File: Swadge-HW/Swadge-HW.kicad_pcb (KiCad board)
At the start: 2 copper layers, 140 x 94.2 mm, 90 parts, among them J1 SAO, J2 PJ-307C, J3 PGM, P1 USB_C_Plug_USB2.0, Q1 Q_PMOS_GSD, SW1 YTS-D003-1A, SW2 YTS-D003-1A, SW3 YTS-D003-1A, SW4 YTS-D003-1A, SW5 YTS-D003-1A, SW6 YTS-D003-1A, SW7 B3FS-4002P, SW8 B3FS-4002P, SW9 SW_SPDT_1825232-1, U1 ESP32-S2-MINI-1, U2 RB017A1505A, U3 MT3410, U5 RB017A1505A_Connector, U6 LSM6DSL, U7 GENERIC_LDO_2.8, U8 FM8002A, U9 INGHAi_GSPK2307P-8R1W

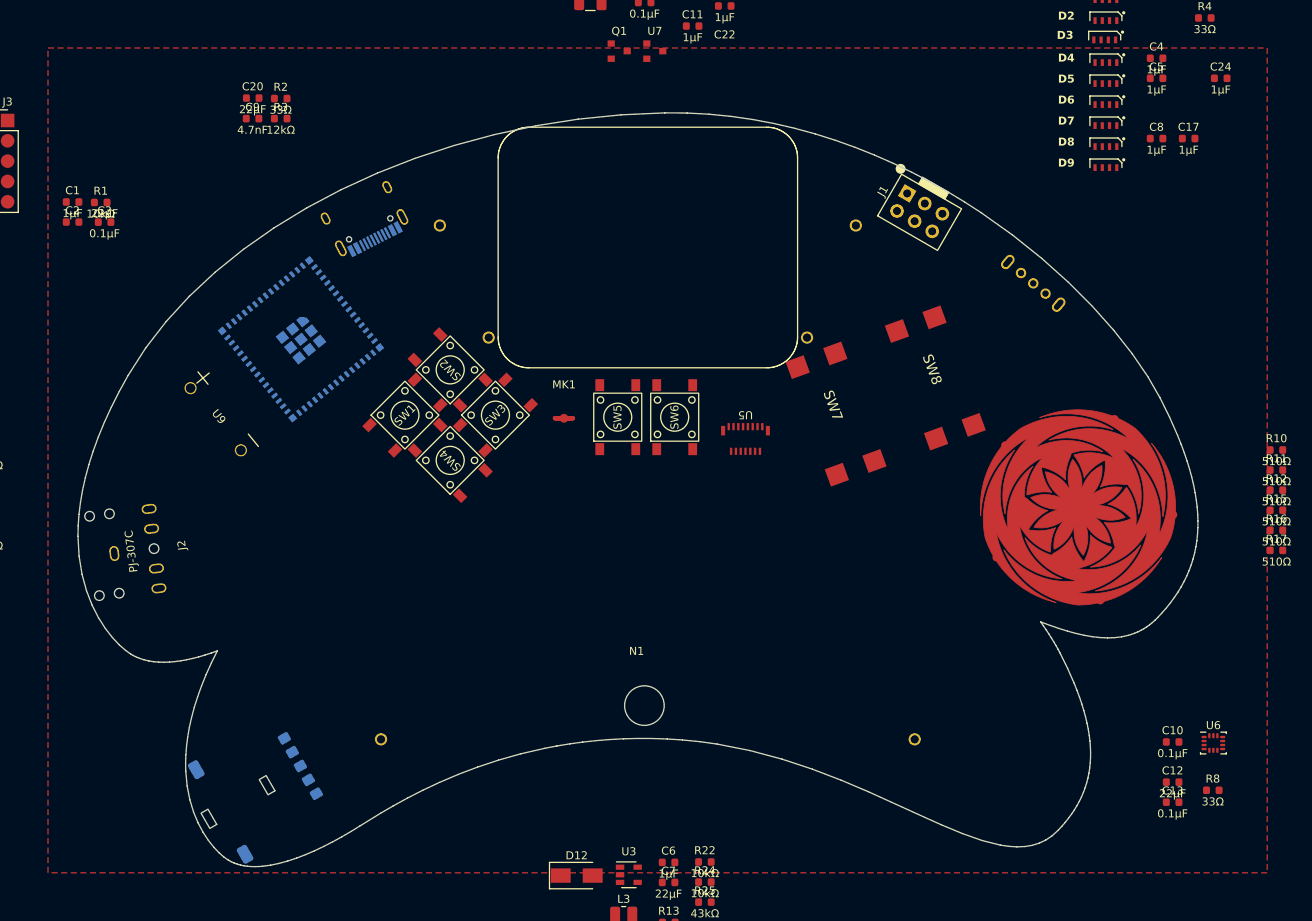
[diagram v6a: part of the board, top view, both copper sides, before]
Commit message: Updated to new board shape
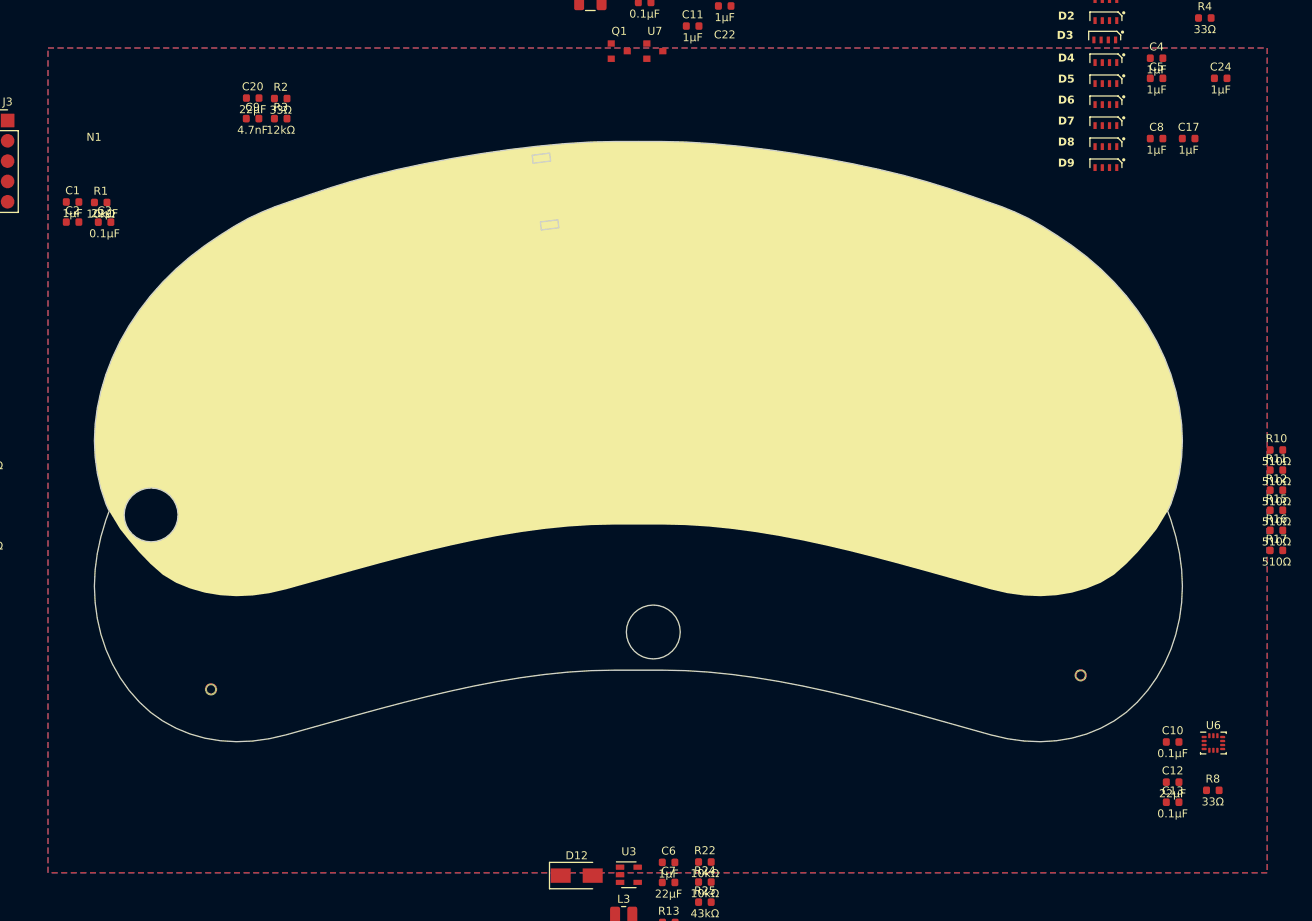
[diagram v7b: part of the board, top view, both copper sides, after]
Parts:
- J2: moved to B.Cu
- N1: value Acrylic Sausage -> Board Outline; footprint Swadge_Hotdog:Sausage -> Swadge_Hotdog:hotdog-outline
- moved N1 93.4 mm to (82.0, 62.4)
- moved RV1 85.4 mm to (138.4, 68.7), turned to -173 degrees
- moved P1 64.0 mm to (179.2, 69.1), turned to -15 degrees
- moved J2 60.0 mm to (124.4, 69.1), turned to -167 degrees
- moved U1 57.1 mm to (163.8, 76.2), turned to 173 degrees
- moved U5 39.1 mm to (139.6, 68.6), turned to 0 degrees
- moved J1 36.3 mm to (147.5, 65.5), turned to 90 degrees
- moved SW6 32.9 mm to (122.0, 101.7), turned to -170 degrees
- moved U9 31.9 mm to (122.0, 77.3), turned to -40 degrees
- moved BT2 28.0 mm to (151.9, 101.0)
- moved SW5 26.9 mm to (123.3, 108.7), turned to -170 degrees
- moved BT3 22.2 mm to (198.6, 104.1)
- moved BT1 22.2 mm to (103.3, 105.9)
- moved SW3 21.0 mm to (111.6, 92.4)
- moved SW2 21.0 mm to (105.9, 86.7)
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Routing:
- added copper zone on B.Cu, net (none)
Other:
- board size 140 x 94.2 mm -> 136 x 75 mm

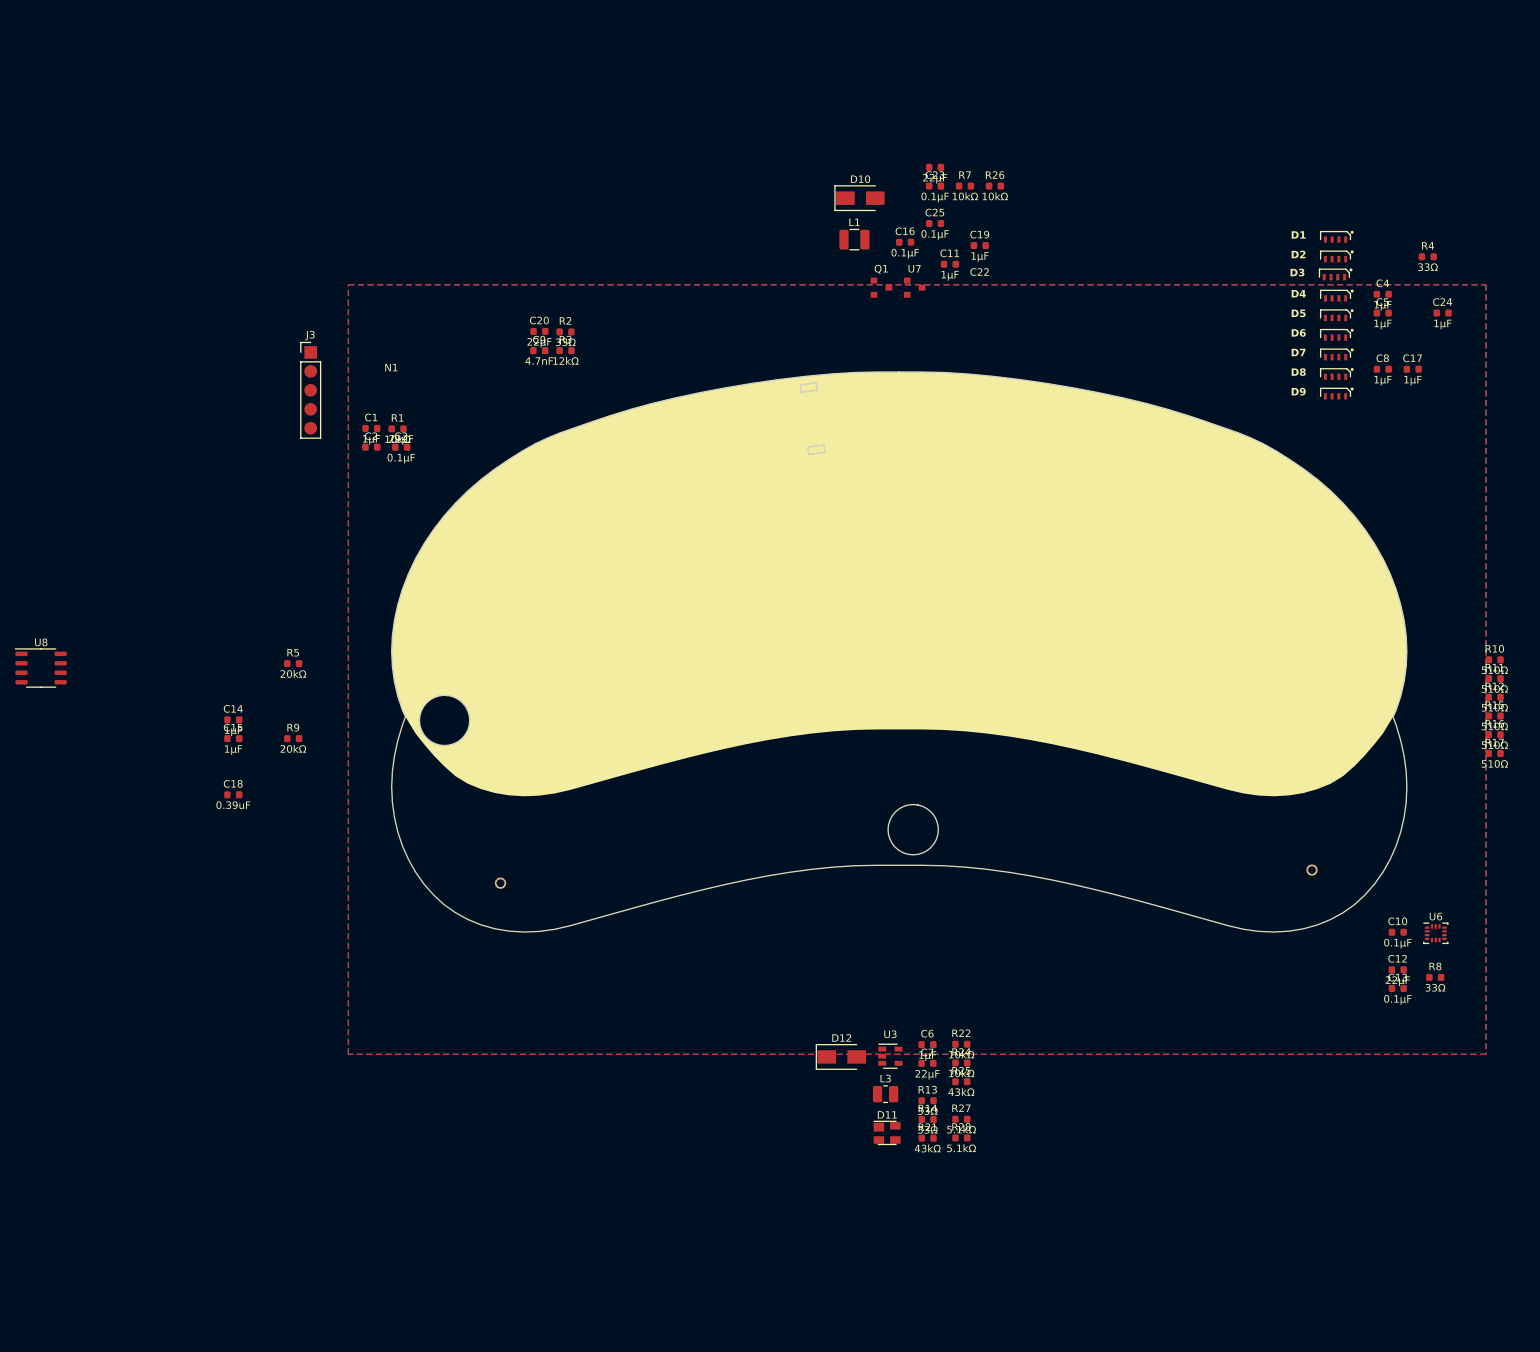
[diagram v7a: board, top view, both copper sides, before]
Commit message: Placed big parts
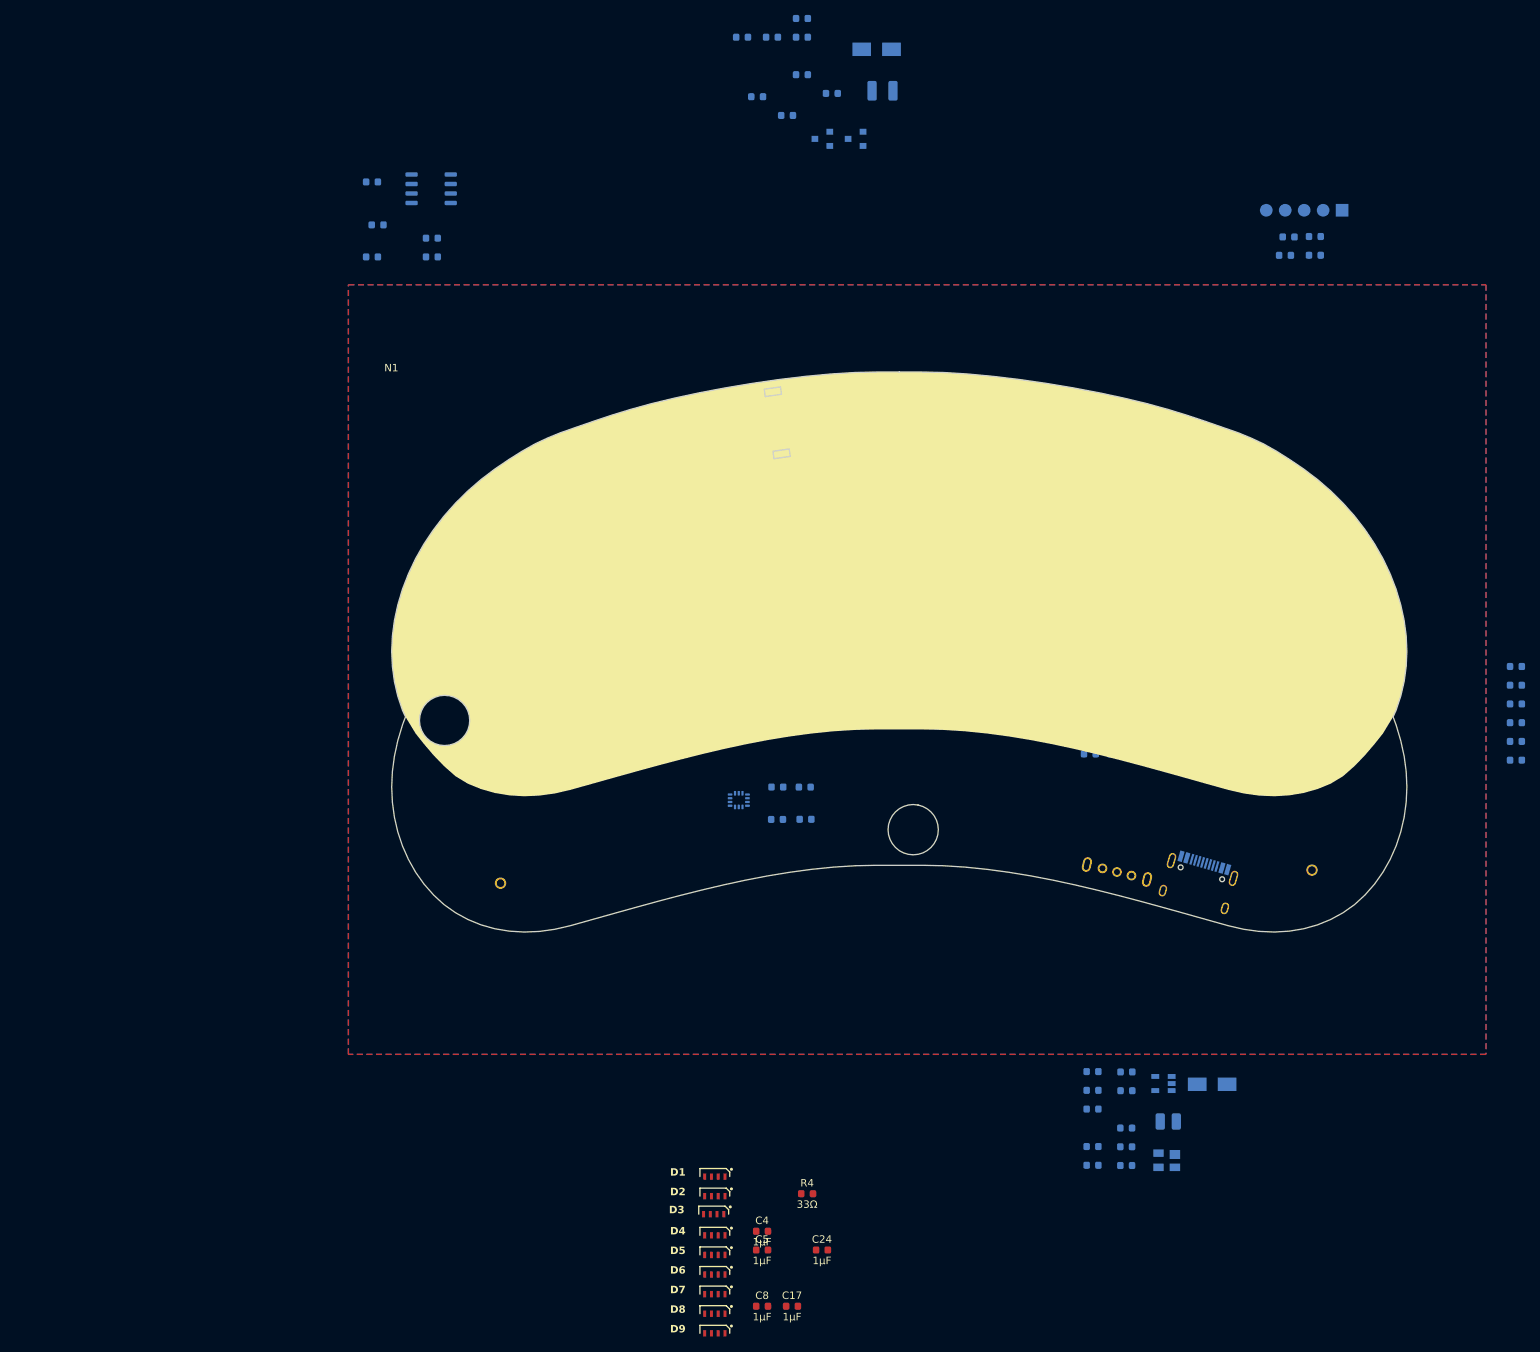
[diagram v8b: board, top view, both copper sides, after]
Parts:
- C1, C10, C11, C12, C13, C14, C15, C16, C18, C19, C2, C20, C22, C23, C25, C3, C6, C7, C9, D10, D11, D12, J3, L1, L3, Q1, R1, R10, R11, R12, R13, R14, R15, R16, R17, R2, R21, R22, R24, R25, R26, R27, R28, R3, R5, R7, R8, R9, U3, U6, U7, U8: moved to B.Cu
- moved C17 150.6 mm to (135.6, 187.6)
- moved C24 150.6 mm to (139.6, 180.1)
- moved C5 150.6 mm to (131.6, 180.1)
- moved D1 150.6 mm to (125.3, 170.3)
- moved D2 150.6 mm to (125.3, 172.9)
- moved D4 150.6 mm to (125.3, 178.1)
- moved D5 150.6 mm to (125.3, 180.8)
- moved D6 150.6 mm to (125.3, 183.4)
- moved D7 150.6 mm to (125.3, 186.0)
- moved D8 150.6 mm to (125.3, 188.6)
- moved D9 150.6 mm to (125.3, 191.3)
- moved C4 150.6 mm to (131.6, 177.6)
- moved C8 150.6 mm to (131.6, 187.6)
- moved D3 150.6 mm to (125.1, 175.3)
- moved R4 150.6 mm to (137.7, 172.6)
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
